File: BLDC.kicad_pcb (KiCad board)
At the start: 4 copper layers, 60 x 60 mm, 122 parts, among them J1 43650-0510, J2 436500313, J3 DNP, J4 43650-0510, J5 BONUS, U1 LMZ21700SIL, U10 INA253, U11 INA253, U12 MCP9808, U13 AS5047U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

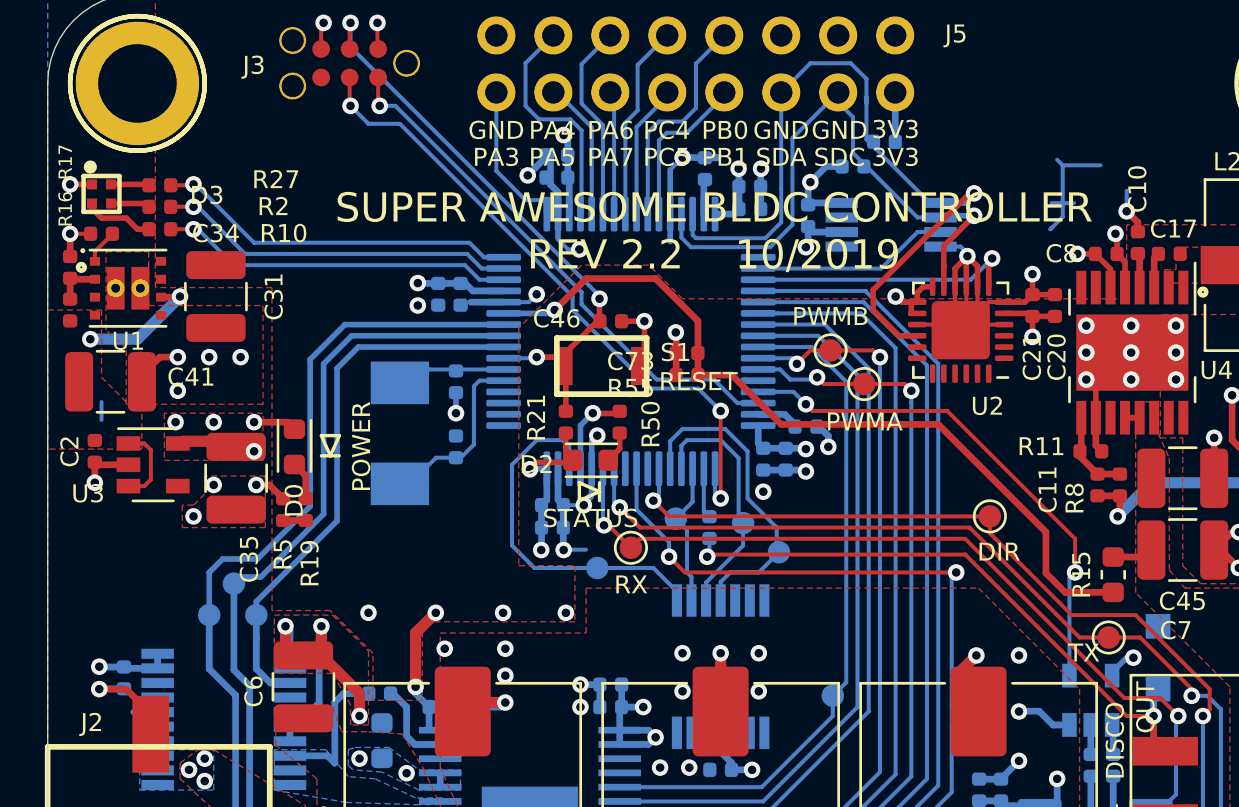
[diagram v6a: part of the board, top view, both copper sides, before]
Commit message: Cosmetic improvements to silkscreen
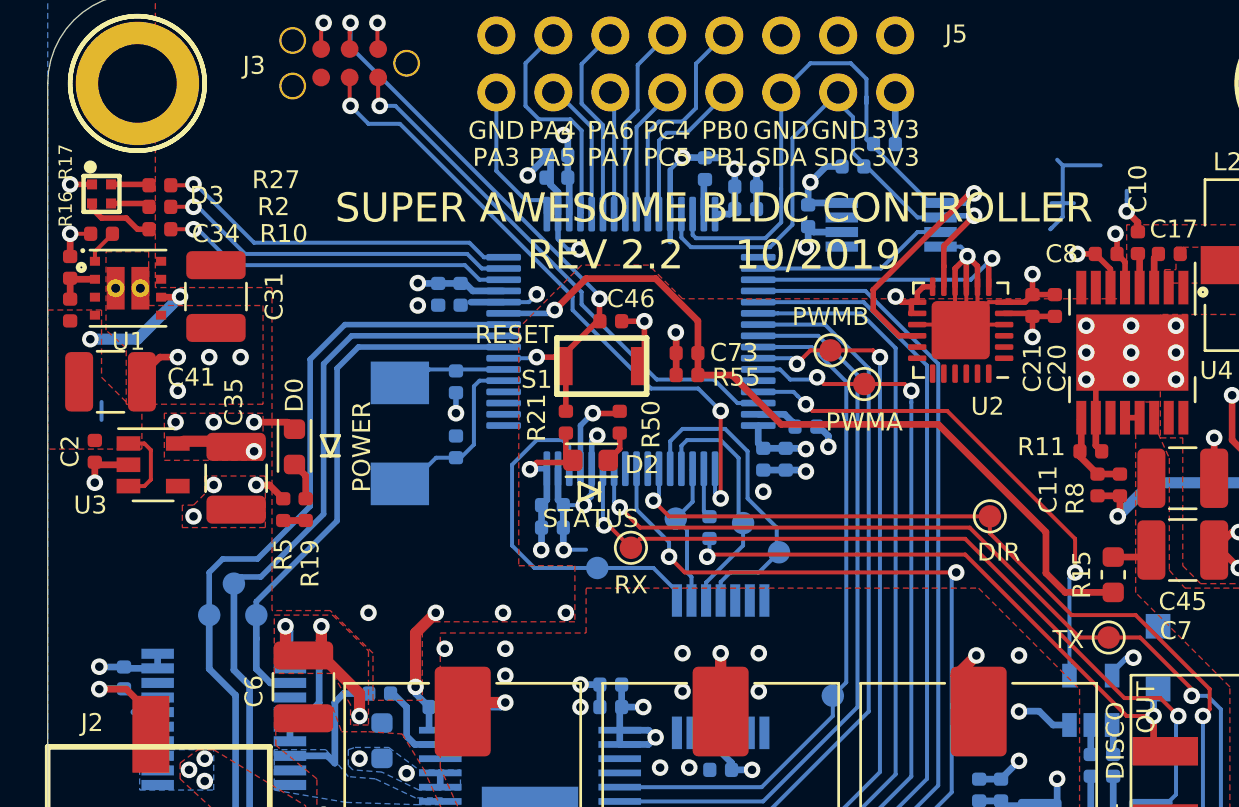
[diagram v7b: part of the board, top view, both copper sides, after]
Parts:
- moved C63 0.19 mm to (149.6, 84.6)
- moved C67 0.19 mm to (149.6, 83.6)
- moved R39 0.10 mm to (155.8, 81.7)

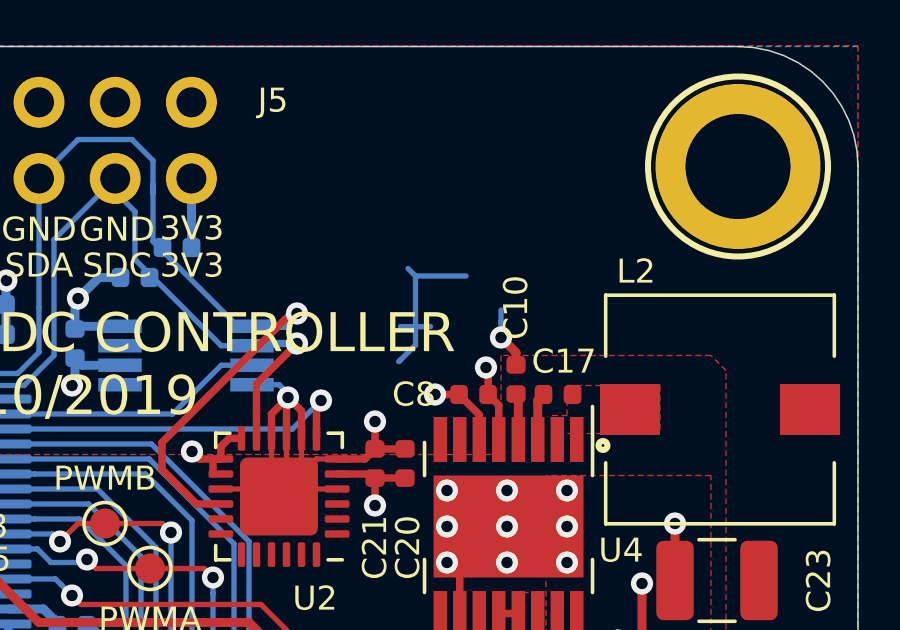
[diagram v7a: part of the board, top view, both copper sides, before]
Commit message: Updated 3d models to include latest inductor
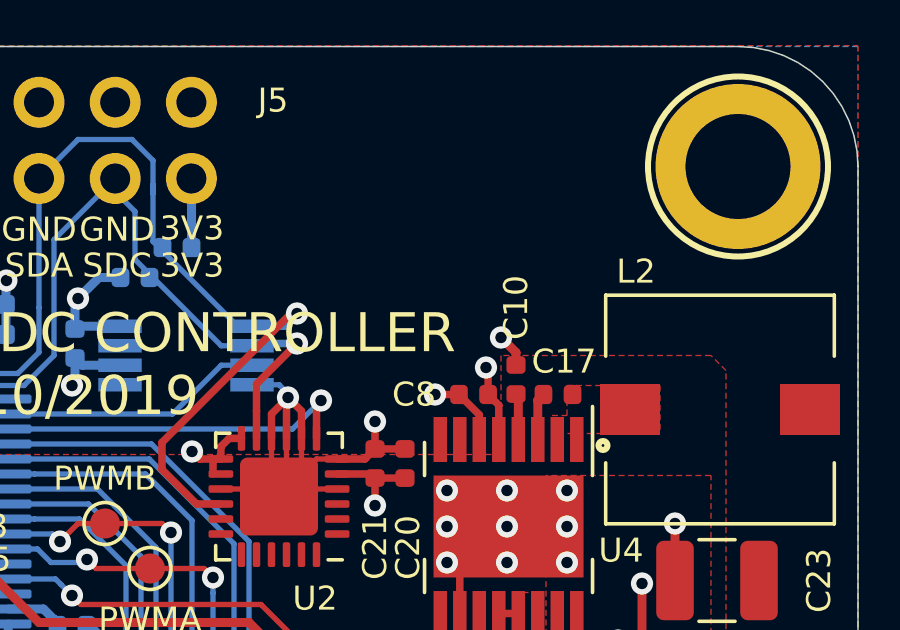
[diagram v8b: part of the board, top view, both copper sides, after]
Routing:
- net GND: track 170.1 -> 163.0 mm
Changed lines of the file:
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@@
     (thickness 1.6)
     (drawings 118)
-    (tracks 1053)
+    (tracks 1043)
     (modules 122)
     (nets 139)
@@
       (rotate (xyz 0 0 0))
     )
+    (model "${KIPRJMOD}/3d_models/STEP-WE-PD-7345-Plastic-rev1.stp"
+      (at (xyz 0 0 0))
+      (scale (xyz 1 1 1))
+      (rotate (xyz 0 0 0))
+    )
   )
   (module "Capacitor_SMD:CP_Elec_10x10" (layer "F.Cu")
@@
   (segment (start 167.176329 88.1) (end 167.176329 86.661329) (width 0.3) (layer "F.Cu") (net 67))
   (segment (start 167.176329 86.661329) (end 167.1 86.585) (width 0.3) (layer "F.Cu") (net 67))
-  (segment (start 163.75 84.3375) (end 163.75 82.65) (width 0.1778) (layer "B.Cu") (net 45))
-  (segment (start 163.75 82.65) (end 163.5 82.4) (width 0.1778) (layer "B.Cu") (net 45))
-  (segment (start 163.25 84.3375) (end 163.75 84.3375) (width 0.1778) (layer "B.Cu") (net 45))
-  (segment (start 163.75 84.3375) (end 163.75 84.95) (width 0.1778) (layer "B.Cu") (net 45))
-  (segment (start 163.75 84.95) (end 163.2 85.5) (width 0.1778) (layer "B.Cu") (net 45))
-  (segment (start 164.25 84.3375) (end 163.75 84.3375) (width 0.1778) (layer "B.Cu") (net 45))
-  (segment (start 163.25 85.45) (end 163.2 85.5) (width 0.1778) (layer "B.Cu") (net 45))
-  (segment (start 165.4375 82.65) (end 163.75 82.65) (width 0.1778) (layer "B.Cu") (net 45))
-  (segment (start 166.599999 84.17674) (end 166.599999 84.699999) (width 0.1778) (layer "B.Cu") (net 45))
   (via (at 166.599999 84.699999) (size 0.74) (drill 0.38) (layers "F.Cu" "B.Cu") (net 45))
-  (segment (start 166.6 83.785) (end 166.599999 84.17674) (width 0.1778) (layer "B.Cu") (net 45))
   (segment (start 157.825 84.325) (end 155 81.5) (width 0.1778) (layer "B.Cu") (net 25))
   (segment (start 158.3 84.325) (end 157.825 84.325) (width 0.1778) (layer "B.Cu") (net 25))
